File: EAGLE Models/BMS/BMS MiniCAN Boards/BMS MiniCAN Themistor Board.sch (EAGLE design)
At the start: 111 parts, among them IC1 AT90CAN128, IC2 MCP2551SO8, IC3 NUP2105L, Q1 56P2859, U1 0ZCH0050FF2G

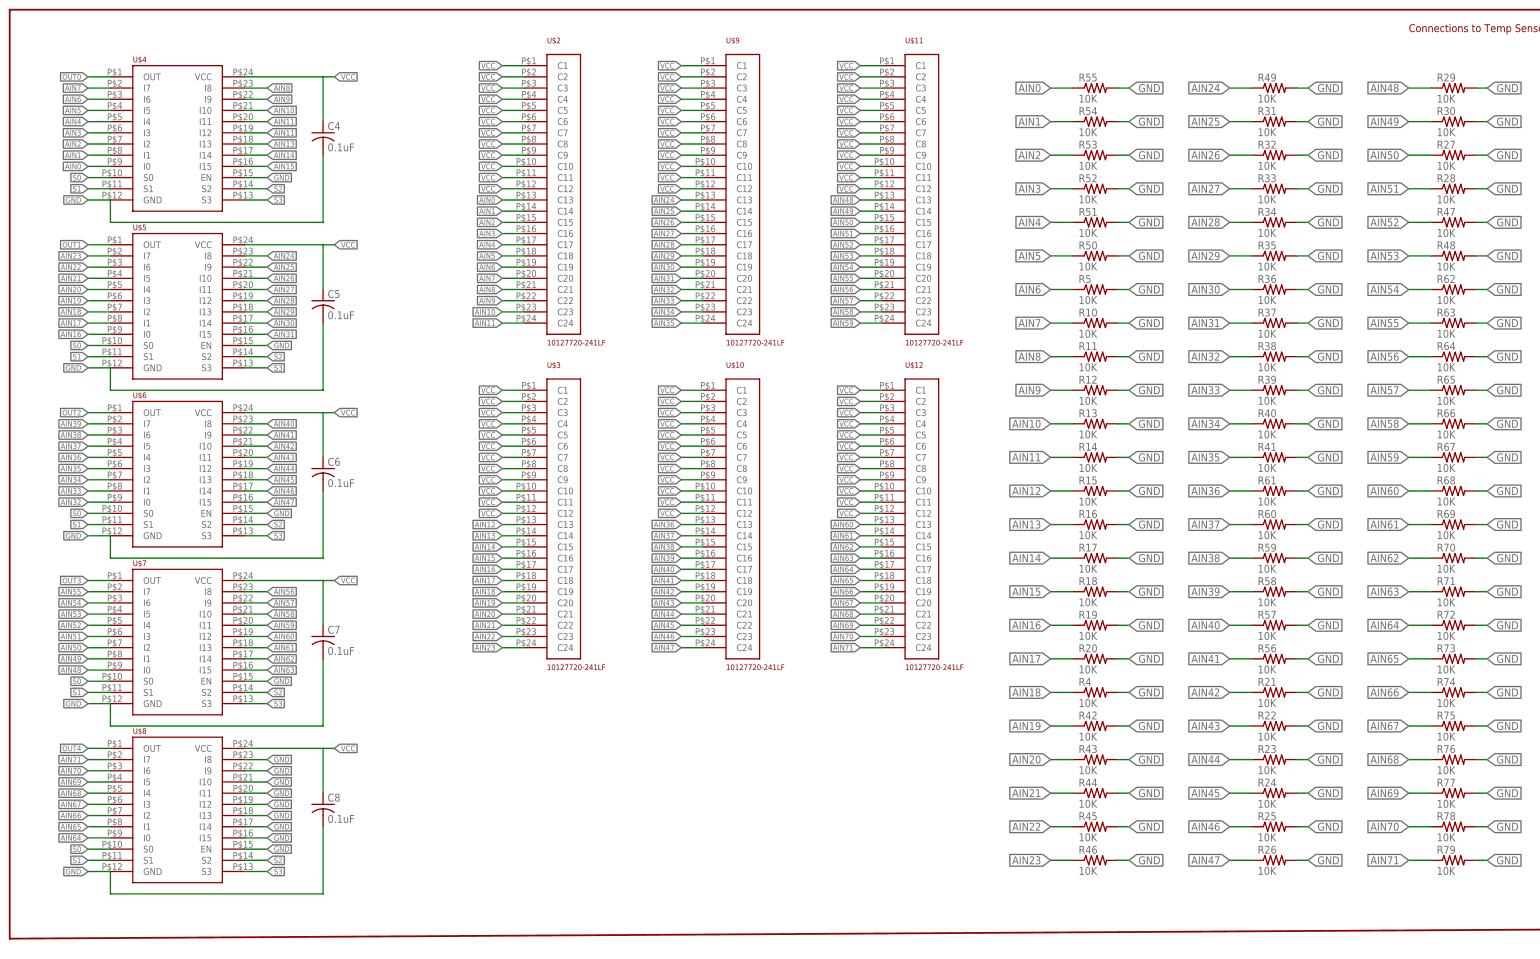
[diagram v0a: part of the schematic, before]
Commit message: Removed old files, did from thermistor connector to mux
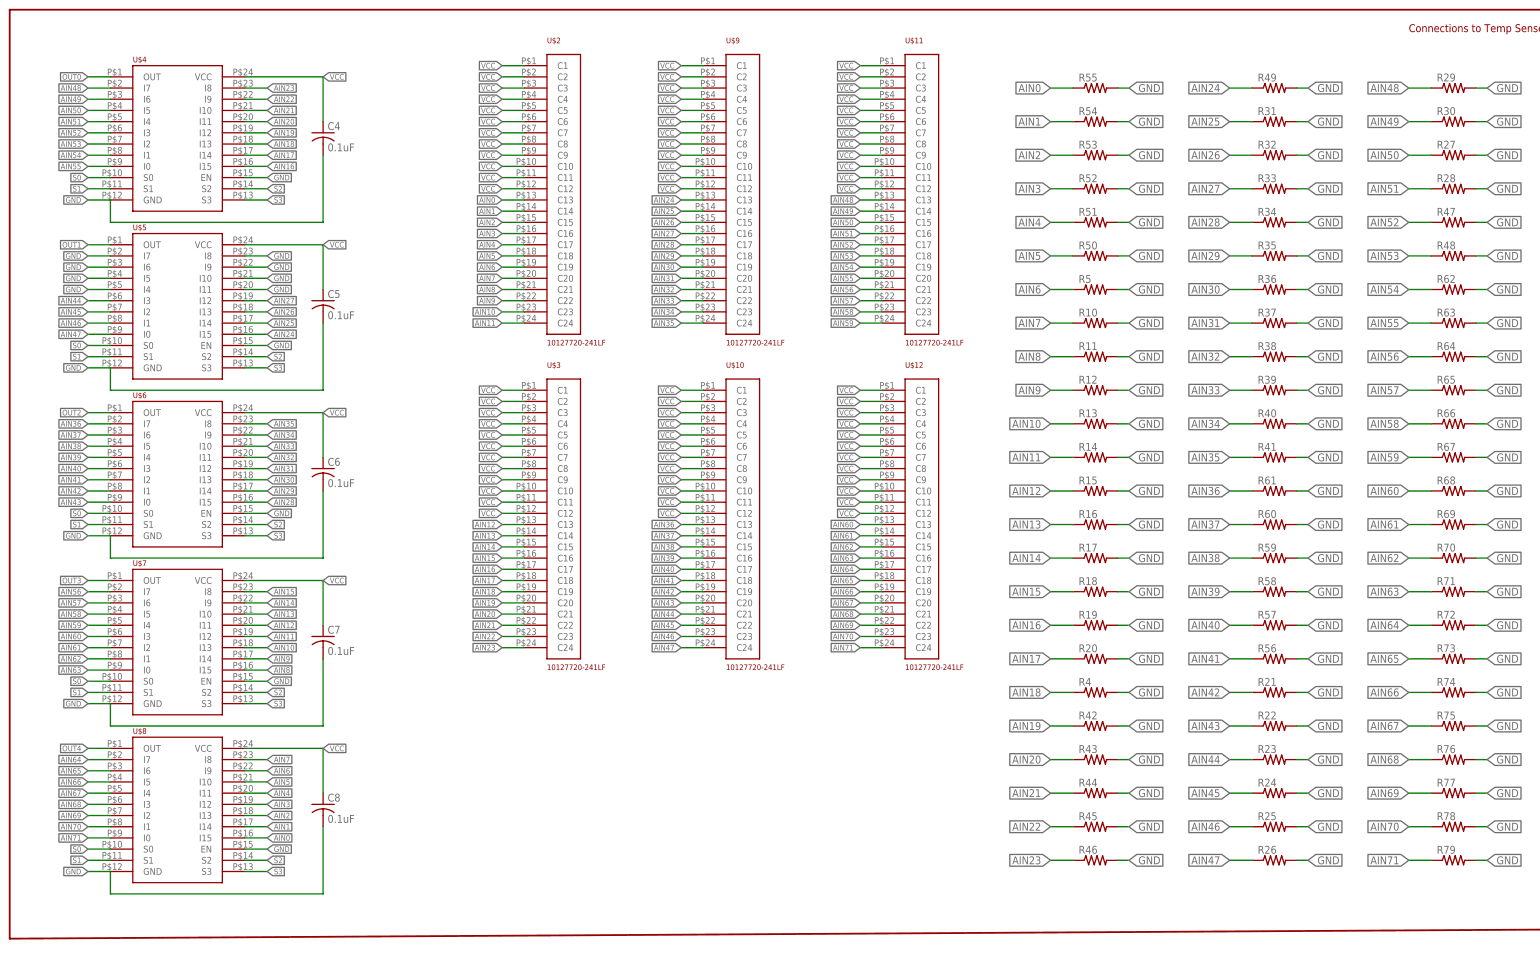
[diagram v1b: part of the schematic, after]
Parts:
- R10, R11, R12, R13, R14, R15, R16, R17, R18, R19, R20, R21, R22, R23, R24, R25, R26, R27, R28, R29, R30, R31, R32, R33, R34, R35, R36, R37, R38, R39, R4, R40, R41, R42, R43, R44, R45, R46, R47, R48, R49, R5, R50, R51, R52, R53, R54, R55, R56, R57, R58, R59, R60, R61, R62, R63, R64, R65, R66, R67, R68, R69, R70, R71, R72, R73, R74, R75, R76, R77, R78, R79: value 10K -> (none)
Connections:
- net AIN0: now also U$8.I15; no longer U$4.I0
- net AIN1: now also U$8.I14; no longer U$4.I1
- net AIN10: now also U$7.I13; no longer U$4.I10
- net AIN11: now also U$7.I12; no longer U$4.I11, U$4.I12
- net AIN12: now also U$7.I11
- net AIN13: now also U$7.I10; no longer U$4.I13
- net AIN14: now also U$7.I9; no longer U$4.I14
- net AIN15: now also U$7.I8; no longer U$4.I15
- net AIN16: now also U$4.I15; no longer U$5.I0
- net AIN17: now also U$4.I14; no longer U$5.I1
- net AIN18: now also U$4.I13; no longer U$5.I2
- net AIN19: now also U$4.I12; no longer U$5.I3
- net AIN2: now also U$8.I13; no longer U$4.I2
- net AIN20: now also U$4.I11; no longer U$5.I4
- net AIN21: now also U$4.I10; no longer U$5.I5
- net AIN22: now also U$4.I9; no longer U$5.I6
- net AIN23: now also U$4.I8; no longer U$5.I7
- net AIN24: now also U$5.I15; no longer U$5.I8
- net AIN25: now also U$5.I14; no longer U$5.I9
- net AIN26: now also U$5.I13; no longer U$5.I10
- net AIN27: now also U$5.I12; no longer U$5.I11
- net AIN28: now also U$6.I15; no longer U$5.I12
- net AIN29: now also U$6.I14; no longer U$5.I13
- net AIN3: now also U$8.I12; no longer U$4.I3
- net AIN30: now also U$6.I13; no longer U$5.I14
- net AIN31: now also U$6.I12; no longer U$5.I15
- net AIN32: now also U$6.I11; no longer U$6.I0
- net AIN33: now also U$6.I10; no longer U$6.I1
- net AIN34: now also U$6.I9; no longer U$6.I2
- net AIN35: now also U$6.I8; no longer U$6.I3
- net AIN36: now also U$6.I7; no longer U$6.I4
- net AIN37: now also U$6.I6; no longer U$6.I5
- net AIN38: now also U$6.I5; no longer U$6.I6
- net AIN39: now also U$6.I4; no longer U$6.I7
- net AIN4: now also U$8.I11; no longer U$4.I4
- net AIN40: now also U$6.I3; no longer U$6.I8
- net AIN41: now also U$6.I2; no longer U$6.I9
- net AIN42: now also U$6.I1; no longer U$6.I10
- net AIN43: now also U$6.I0; no longer U$6.I11
- net AIN44: now also U$5.I3; no longer U$6.I12
- net AIN45: now also U$5.I2; no longer U$6.I13
- net AIN46: now also U$5.I1; no longer U$6.I14
- net AIN47: now also U$5.I0; no longer U$6.I15
- net AIN48: now also U$4.I7; no longer U$7.I0
- net AIN49: now also U$4.I6; no longer U$7.I1
- net AIN5: now also U$8.I10; no longer U$4.I5
- net AIN50: now also U$4.I5; no longer U$7.I2
- net AIN51: now also U$4.I4; no longer U$7.I3
- net AIN52: now also U$4.I3; no longer U$7.I4
- net AIN53: now also U$4.I2; no longer U$7.I5
- net AIN54: now also U$4.I1; no longer U$7.I6
- net AIN55: now also U$4.I0; no longer U$7.I7
- net AIN56: now also U$7.I7; no longer U$7.I8
- net AIN57: now also U$7.I6; no longer U$7.I9
- net AIN58: now also U$7.I5; no longer U$7.I10
- net AIN59: now also U$7.I4; no longer U$7.I11
- net AIN6: now also U$8.I9; no longer U$4.I6
- net AIN60: now also U$7.I3; no longer U$7.I12
- net AIN61: now also U$7.I2; no longer U$7.I13
- net AIN62: now also U$7.I1; no longer U$7.I14
- net AIN63: now also U$7.I0; no longer U$7.I15
- net AIN64: now also U$8.I7; no longer U$8.I0
- net AIN65: now also U$8.I6; no longer U$8.I1
- net AIN66: now also U$8.I5; no longer U$8.I2
- net AIN67: now also U$8.I4; no longer U$8.I3
- net AIN68: now also U$8.I3; no longer U$8.I4
- net AIN69: now also U$8.I2; no longer U$8.I5
- net AIN7: now also U$8.I8; no longer U$4.I7
- net AIN70: now also U$8.I1; no longer U$8.I6
- net AIN71: now also U$8.I0; no longer U$8.I7
- net AIN8: now also U$7.I15; no longer U$4.I8
- net AIN9: now also U$7.I14; no longer U$4.I9
- net GND: now also U$5.I10, U$5.I11, U$5.I4, U$5.I5, U$5.I6, U$5.I7, U$5.I8, U$5.I9; no longer U$8.I10, U$8.I11, U$8.I12, U$8.I13, U$8.I14, U$8.I15, U$8.I8, U$8.I9
- net VCC: now also U$5.VCC, U$6.VCC, U$7.VCC, U$8.VCC

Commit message: Added Select Vias
Added select vias, still need the output vias from the muxes.
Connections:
- removed net PE2: IC1.(XCK0/AIN0)PE2
- removed net PE3(PWM): IC1.(OC3A/AIN1)PE3
- removed net PE4(PWM): IC1.(OC3B/INT4)PE4
- removed net PE5(PWM): IC1.(OC3C/INT5)PE5
- net S0: now also IC1.(OC3A/AIN1)PE3; no longer IC1.(A8)PC0
- net S1: now also IC1.(XCK0/AIN0)PE2; no longer IC1.(A9)PC1
- net S2: now also IC1.(OC3B/INT4)PE4; no longer IC1.(A10)PC2
- net S3: now also IC1.(OC3C/INT5)PE5; no longer IC1.(A11)PC3
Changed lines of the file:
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@@
-</segment>
-</net>
-<net name="PE2" class="0">
-<segment>
-<wire x1="373.38" y1="71.12" x2="368.3" y2="71.12" width="0.1524" layer="91"/>
-<label x="370.84" y="71.12" size="1.778" layer="95"/>
-<pinref part="IC1" gate="G$1" pin="(XCK0/AIN0)PE2"/>
 </segment>
 </net>
@@
 </segment>
 </net>
-<net name="PE5(PWM)" class="0">
-<segment>
-<wire x1="373.38" y1="78.74" x2="368.3" y2="78.74" width="0.1524" layer="91"/>
-<label x="370.84" y="78.74" size="1.778" layer="95"/>
-<pinref part="IC1" gate="G$1" pin="(OC3C/INT5)PE5"/>
-</segment>
-</net>
-<net name="PE4(PWM)" class="0">
-<segment>
-<wire x1="373.38" y1="76.2" x2="368.3" y2="76.2" width="0.1524" layer="91"/>
-<label x="370.84" y="76.2" size="1.778" layer="95"/>
-<pinref part="IC1" gate="G$1" pin="(OC3B/INT4)PE4"/>
-</segment>
-</net>
-<net name="PE3(PWM)" class="0">
-<segment>
-<wire x1="373.38" y1="73.66" x2="368.3" y2="73.66" width="0.1524" layer="91"/>
-<label x="370.84" y="73.66" size="1.778" layer="95"/>
-<pinref part="IC1" gate="G$1" pin="(OC3A/AIN1)PE3"/>
-</segment>
-</net>
 <net name="PG0" class="0">
 <segment>
@@
 </segment>
 <segment>
-<wire x1="373.38" y1="116.84" x2="368.3" y2="116.84" width="0.1524" layer="91"/>
-<label x="370.84" y="116.84" size="1.778" layer="95"/>
-<pinref part="IC1" gate="G$1" pin="(A10)PC2"/>
-<label x="373.38" y="116.84" size="1.016" layer="95" xref="yes"/>
+<pinref part="IC1" gate="G$1" pin="(OC3B/INT4)PE4"/>
+<wire x1="368.3" y1="76.2" x2="373.38" y2="76.2" width="0.1524" layer="91"/>
+<label x="373.38" y="76.2" size="1.27" layer="95" xref="yes"/>
 </segment>
 </net>
@@
 </segment>
 <segment>
-<wire x1="373.38" y1="119.38" x2="368.3" y2="119.38" width="0.1524" layer="91"/>
-<label x="370.84" y="119.38" size="1.778" layer="95"/>
-<pinref part="IC1" gate="G$1" pin="(A11)PC3"/>
-<label x="373.38" y="119.38" size="1.016" layer="95" xref="yes"/>
+<pinref part="IC1" gate="G$1" pin="(OC3C/INT5)PE5"/>
+<wire x1="368.3" y1="78.74" x2="373.38" y2="78.74" width="0.1524" layer="91"/>
+<label x="373.38" y="78.74" size="1.27" layer="95" xref="yes"/>
 </segment>
 </net>
@@
 </segment>
 <segment>
-<wire x1="373.38" y1="111.76" x2="368.3" y2="111.76" width="0.1524" layer="91"/>
-<label x="370.84" y="111.76" size="1.778" layer="95"/>
-<pinref part="IC1" gate="G$1" pin="(A8)PC0"/>
-<label x="373.38" y="111.76" size="1.016" layer="95" xref="yes"/>
+<pinref part="IC1" gate="G$1" pin="(OC3A/AIN1)PE3"/>
+<wire x1="368.3" y1="73.66" x2="373.38" y2="73.66" width="0.1524" layer="91"/>
+<label x="373.38" y="73.66" size="1.27" layer="95" xref="yes"/>
 </segment>
 </net>
@@
 </segment>
 <segment>
-<wire x1="373.38" y1="114.3" x2="368.3" y2="114.3" width="0.1524" layer="91"/>
-<label x="370.84" y="114.3" size="1.778" layer="95"/>
-<pinref part="IC1" gate="G$1" pin="(A9)PC1"/>
-<label x="373.38" y="114.3" size="1.016" layer="95" xref="yes"/>
-</segment>
-</net>
+<pinref part="IC1" gate="G$1" pin="(XCK0/AIN0)PE2"/>
+<wire x1="368.3" y1="71.12" x2="373.38" y2="71.12" width="0.1524" layer="91"/>
+<label x="373.38" y="71.12" size="1.27" layer="95" xref="yes"/>
+</segment>
+</net>

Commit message: Added Vias and traces for the right side of the board
Added vias for the selects and outputs. Added most of the traces for the
right side of the board except for a 12V trace that might be a problem.
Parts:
- D2: value 1N5819 -> DFLS1100; device diode:1N5819-B -> BMS Lbr:DFLS1100
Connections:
- net 12V: now also D2.22; no longer D2.A
- net AVR_SCK: now also H7.5; no longer H7.3
- net CAN_H: now also X1/4.$/1; no longer X1/3.$/1
- net CAN_L: now also X1/3.$/1; no longer X1/4.$/1
- net N$1: now also D2.11; no longer D2.C
- net RESET: now also H7.3; no longer H7.5
- net RX: now also H7.2; no longer H7.4
- net TX: now also H7.4; no longer H7.1
- net VCC: now also H7.1; no longer H7.2
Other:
- moved on the sheet: D2

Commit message: Improved Board
Improved ground connections, needs more improvement.
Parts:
- removed H7: ICSP, SparkFun-Connectors:M03X2SMD_FCI
- removed X1: (no value), BMS Lbr:4_PIN_CONN
- added C10: 0.1uF, rcl:C-USC0805
- added ISP1: AVRISP-6, adafruit:AVRISP-6
- added U$13: 0039300040, BMS Lbr:0039300040
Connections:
- removed net N$22: IC1.AVCC, L1.2
- new net N$3: C10.2, IC1.AREF
- net 12V: now also U$13.P$1; no longer X1/1.$/1
- net AREF: now also IC1.AVCC, L1.2; no longer IC1.AREF
- net AVR_SCK: now also ISP1.SCK; no longer H7.5
- net CAN_H: now also U$13.P$4; no longer X1/4.$/1
- net CAN_L: now also U$13.P$3; no longer X1/3.$/1
- net GND: now also C10.1, ISP1.GND; no longer H7.6
- net N$2: now also U$13.P$2; no longer X1/2.$/1
- net RESET: now also ISP1.RST; no longer H7.3
- net RX: now also ISP1.MISO; no longer H7.2
- net S0: now also IC1.(A11)PC3; no longer IC1.(OC3A/AIN1)PE3
- net S1: now also IC1.(A10)PC2; no longer IC1.(XCK0/AIN0)PE2
- net S2: now also IC1.(A9)PC1; no longer IC1.(OC3B/INT4)PE4
- net S3: now also IC1.(A8)PC0; no longer IC1.(OC3C/INT5)PE5
- net TX: now also ISP1.MOSI; no longer H7.4
- net VCC: now also ISP1.VCC; no longer H7.1
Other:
- moved on the sheet: L1
